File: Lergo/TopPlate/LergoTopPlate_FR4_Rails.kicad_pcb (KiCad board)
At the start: 2 copper layers, 164 x 146.3 mm, 38 parts, among them SW2 KEY_SWITCH, SW2 PRO MICRO

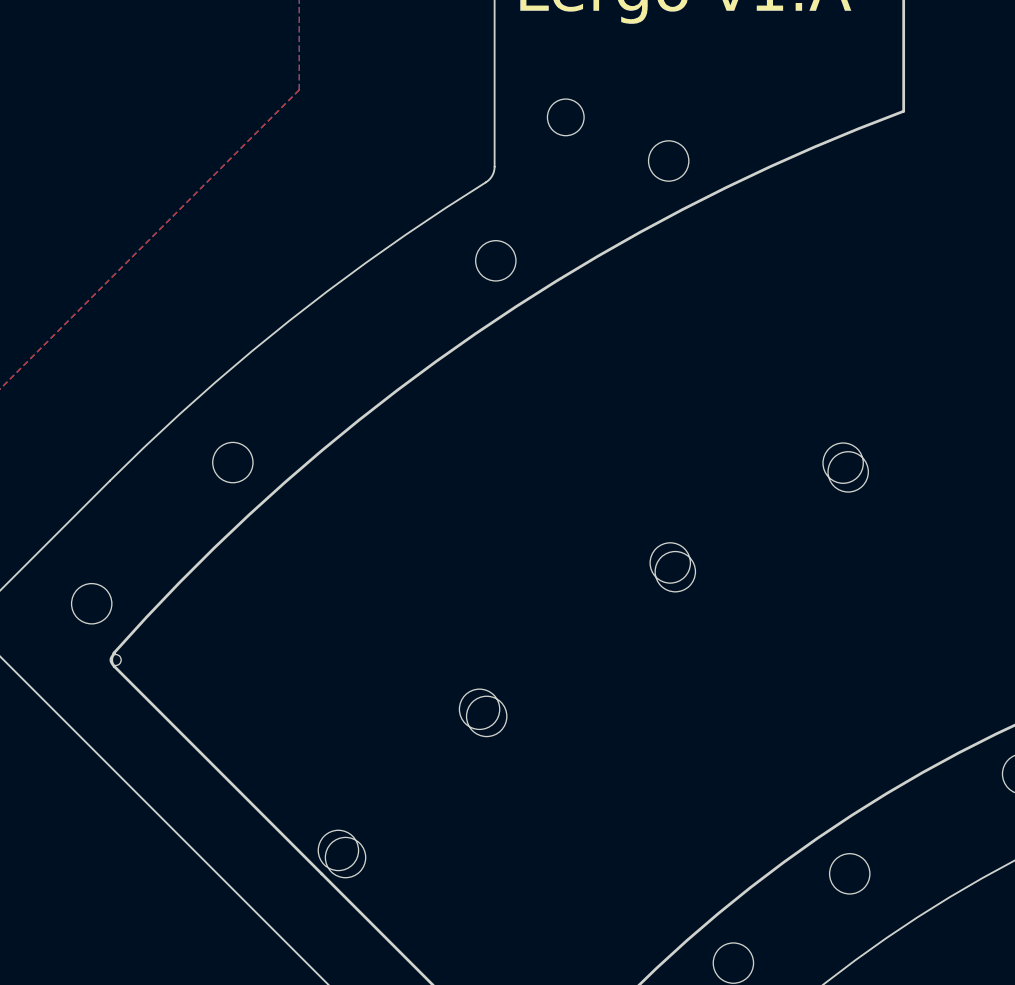
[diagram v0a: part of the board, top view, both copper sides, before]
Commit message: Fixing some issues in some FR4 top plates found while doing the Alu modifications earlier (not complete yet)
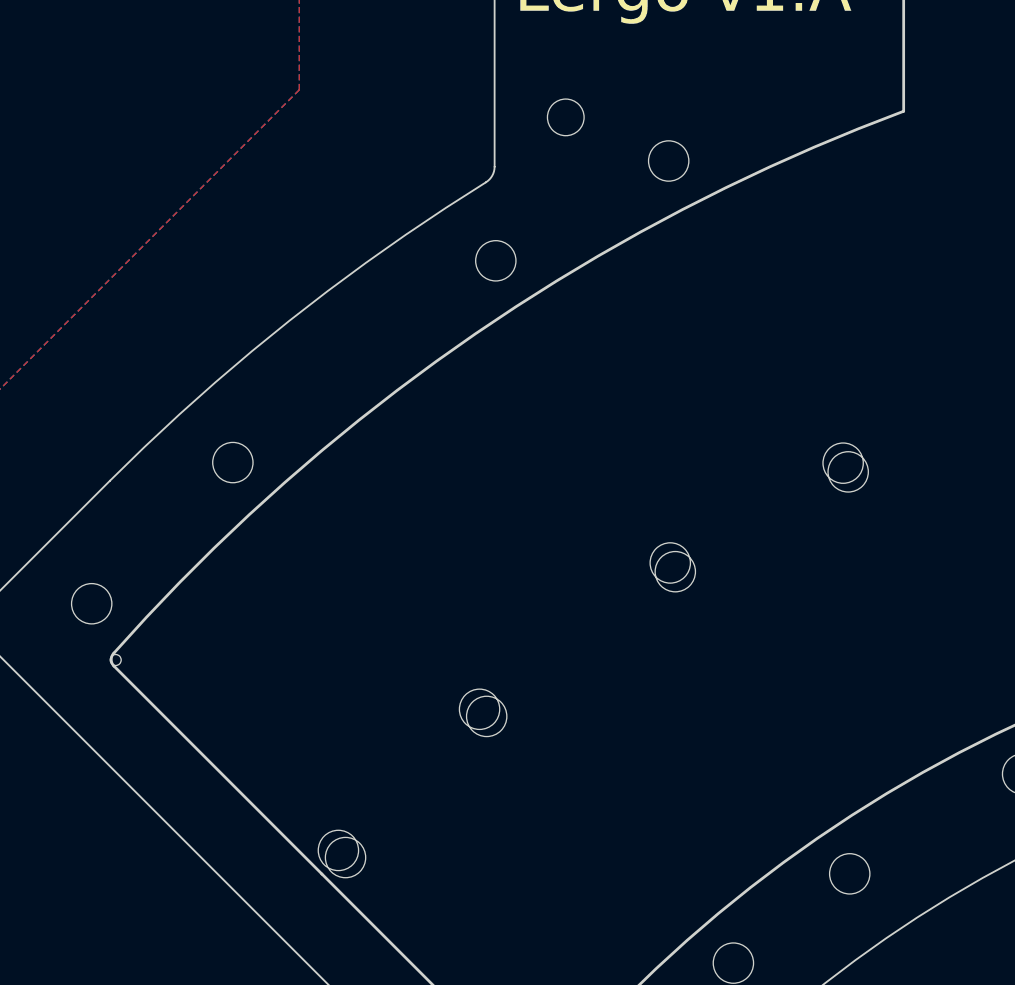
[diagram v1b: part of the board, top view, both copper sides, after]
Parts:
- moved REF** 9.48 mm to (188.1, 118.1)
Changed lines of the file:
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@@
   (general
     (thickness 1.6)
-    (drawings 154)
+    (drawings 153)
     (tracks 0)
     (zones 0)
@@
     (uvia_drill 0.1)
   )
+  (module "Lergo Footprints:CherryMX_Lergo_v1_TopPlate_Corner" (layer F.Cu)
+    (at 188.1 118.12)
+    (fp_text reference REF** (at 0 2.7) (layer F.Fab) hide
+      (effects (font (size 1 1) (thickness 0.15)))
+    )
+    (fp_text value CherryMX_Kyfle_v1_TopPlate_Corner (at 0.1 -3.3) (layer F.Fab) hide
+      (effects (font (size 1 1) (thickness 0.15)))
+    )
+    (pad "" np_thru_hole circle (at 6.7 6.7) (size 0.6 0.6) (drill 0.6) (layers *.Cu))
+  )
   (module "Lergo Footprints:CherryMX_Lergo_v1_TopPlate_2u_1u_Rail_End" (layer F.Cu)
     (at 97.135413 135.364647 45)
@@
     (fp_line (start -6.5 16.525) (end 0 16.525) (layer Edge.Cuts) (width 0.15))
     (fp_line (start -7 0) (end -7 16.025) (layer Edge.Cuts) (width 0.15))
-    (fp_line (start -7 -16.025) (end -7 0) (layer Edge.Cuts) (width 0.15))
+    (fp_line (start -7 -16.060048) (end -7 0) (layer Edge.Cuts) (width 0.15))
+    (fp_text user VCC (at -5.334 4.0005 45) (layer B.Fab)
+      (effects (font (size 1 1) (thickness 0.15)))
+    )
+    (fp_text user GND (at 3.048 6.2865 45) (layer B.Fab)
+      (effects (font (size 1 1) (thickness 0.15)))
+    )
+    (fp_text user DOUT (at -4.0005 6.2865 45) (layer B.Fab)
+      (effects (font (size 1 1) (thickness 0.15)))
+    )
+    (fp_text user DIN (at -4.0005 -9.3345 45) (layer B.Fab)
+      (effects (font (size 1 1) (thickness 0.15)))
+    )
+    (fp_text user COL (at -5.5245 -4.0005 45) (layer B.Fab)
+      (effects (font (size 1 1) (thickness 0.15)))
+    )
+    (fp_text user ROW (at -0.381 -6.096 45) (layer B.Fab)
+      (effects (font (size 1 1) (thickness 0.15)))
+    )
+    (fp_text user "Small hole = pinch side" (at -21.43125 -11.90625 45) (layer Cmts.User)
+      (effects (font (size 1 1) (thickness 0.15)))
+    )
+    (fp_text user "Big hole = wire side" (at 23.8125 -9.525 45) (layer Cmts.User)
+      (effects (font (size 1 1) (thickness 0.15)))
+    )
     (fp_text user "Small hole = pinch/screw side" (at -26.19375 -11.90625 45) (layer Cmts.User)
-      (effects (font (size 1 1) (thickness 0.15)))
-    )
-    (fp_text user "Big hole = wire side" (at 23.8125 -9.525 45) (layer Cmts.User)
-      (effects (font (size 1 1) (thickness 0.15)))
-    )
-    (fp_text user "Small hole = pinch side" (at -21.43125 -11.90625 45) (layer Cmts.User)
-      (effects (font (size 1 1) (thickness 0.15)))
-    )
-    (fp_text user ROW (at -0.381 -6.096 45) (layer B.Fab)
-      (effects (font (size 1 1) (thickness 0.15)))
-    )
-    (fp_text user COL (at -5.5245 -4.0005 45) (layer B.Fab)
-      (effects (font (size 1 1) (thickness 0.15)))
-    )
-    (fp_text user DIN (at -4.0005 -9.3345 45) (layer B.Fab)
-      (effects (font (size 1 1) (thickness 0.15)))
-    )
-    (fp_text user DOUT (at -4.0005 6.2865 45) (layer B.Fab)
-      (effects (font (size 1 1) (thickness 0.15)))
-    )
-    (fp_text user GND (at 3.048 6.2865 45) (layer B.Fab)
-      (effects (font (size 1 1) (thickness 0.15)))
-    )
-    (fp_text user VCC (at -5.334 4.0005 45) (layer B.Fab)
       (effects (font (size 1 1) (thickness 0.15)))
     )
@@
       (effects (font (size 1 1) (thickness 0.15)))
     )
-    (fp_arc (start -6.5 -16.025) (end -6.5 -16.525) (angle -90) (layer Edge.Cuts) (width 0.15))
+    (fp_arc (start -6.5 -16.060048) (end -6.5 -16.560048) (angle -90) (layer Edge.Cuts) (width 0.15))
     (fp_text user KEY_SWITCH (at 0 -13.525 45) (layer F.Fab) hide
       (effects (font (size 1 1) (thickness 0.15)))
@@
     )
   )
-  (module "Lergo Footprints:CherryMX_Lergo_v1_TopPlate_Corner" (layer F.Cu)
-    (at 194.8 124.82)
-    (fp_text reference REF** (at 0 2.7) (layer F.Fab) hide
-      (effects (font (size 1 1) (thickness 0.15)))
-    )
-    (fp_text value CherryMX_Kyfle_v1_TopPlate_Corner (at 0.1 -3.3) (layer F.Fab) hide
-      (effects (font (size 1 1) (thickness 0.15)))
-    )
-    (pad "" np_thru_hole circle (at 0 0) (size 0.6 0.6) (drill 0.6) (layers *.Cu *.Mask))
-  )
   (module "Lergo Footprints:CherryMX_Lergo_v1_TopPlate_1u_Rail_Helper" (layer F.Cu)
     (at 130.95 108.59 180)
@@
   (gr_line (start 235.725 125.04375) (end 235.725 44.27625) (layer F.SilkS) (width 0.15))
   (gr_line (start 137.95 109.342358) (end 139.444588 113.682955) (layer Edge.Cuts) (width 0.15))
-  (gr_line (start 80.83067 128.2497) (end 80.854279 128.275902) (layer Edge.Cuts) (width 0.15))
-  (gr_arc (start 161.760381 199.9936) (end 123.95 98.666504) (angle -27.97997949) (layer Edge.Cuts) (width 0.15))
+  (gr_arc (start 161.760381 199.9936) (end 123.95 98.666504) (angle -27.98095428) (layer Edge.Cuts) (width 0.15))
   (gr_line (start 154.760001 111.120001) (end 181.1 111.12) (layer Edge.Cuts) (width 0.15))
   (gr_arc (start 194.6 124.62) (end 194.6 125.12) (angle -90) (layer Edge.Cuts) (width 0.15))
